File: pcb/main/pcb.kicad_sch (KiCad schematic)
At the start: 45 parts, among them J1 Conn_01x04, J2 USB_B_Micro, J6 Barrel_Jack_MountingPin, Q1 Q_NMOS_GDS, Q3 Q_NMOS_GDS, U2 ESP32-C3-WROOM-02, U5 IX4427N, U6 LMR54406DBVR

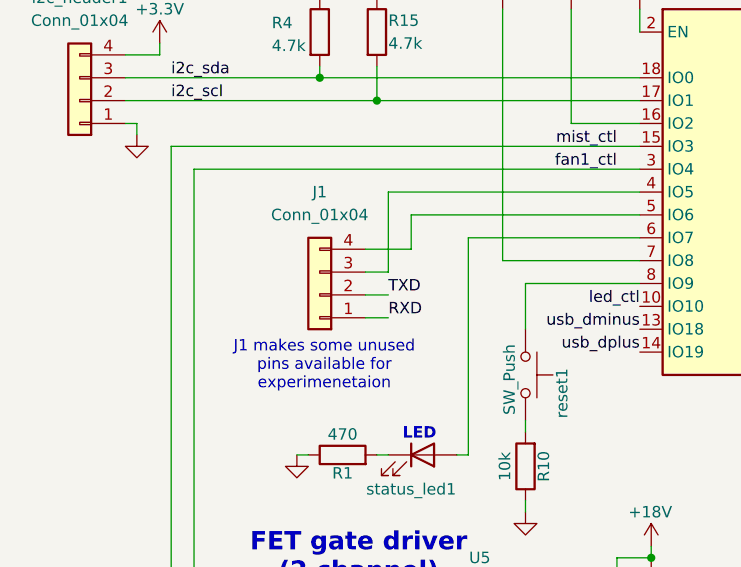
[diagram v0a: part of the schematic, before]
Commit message: pcb: mark debug header as "do not place" and add a part number for i2c header
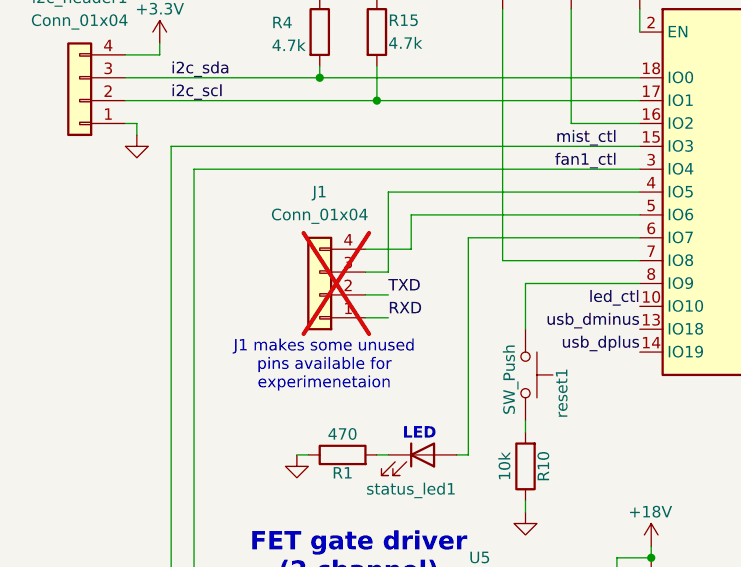
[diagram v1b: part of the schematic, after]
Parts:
- J1: now not fitted; now left out of the parts list
- i2c_header1: LCSC Part # (none) -> C124378
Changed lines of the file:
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@@
+			)
+		)
+		(property "LCSC Part #" "C124378"
+			(at 27.94 83.82 0)
+			(effects
+				(font
+					(size 1.27 1.27)
+				)
+				(hide yes)
 			)
 		)
@@
 		(unit 1)
 		(exclude_from_sim no)
-		(in_bom yes)
-		(on_board yes)
-		(dnp no)
+		(in_bom no)
+		(on_board yes)
+		(dnp yes)
 		(fields_autoplaced yes)
 		(property "Reference" "J1"

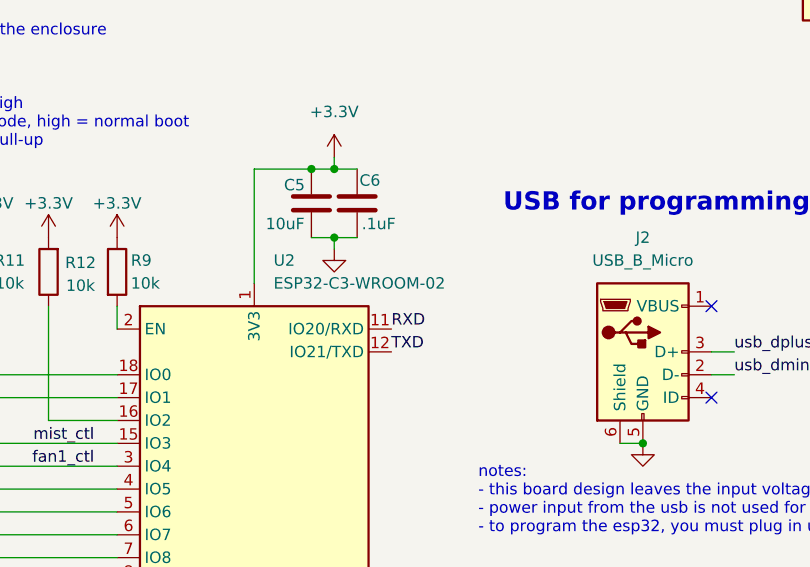
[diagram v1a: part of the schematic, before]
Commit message: pcb: update part # for esp32
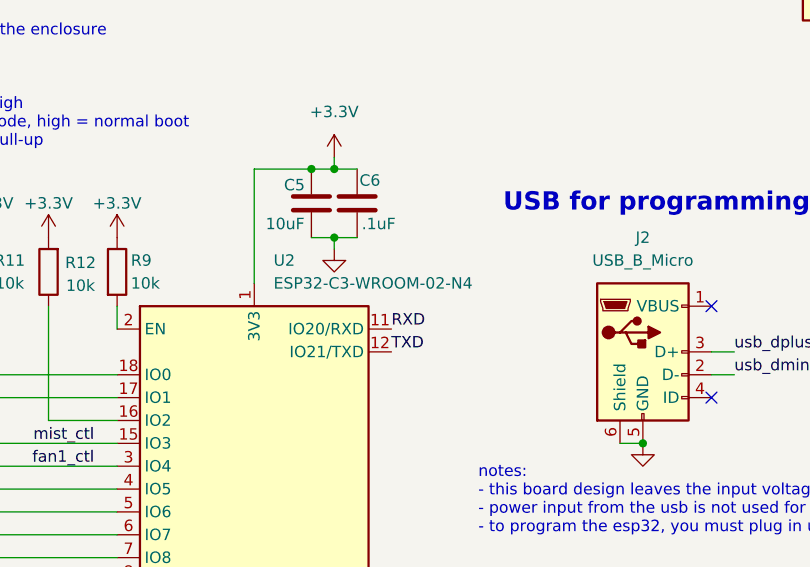
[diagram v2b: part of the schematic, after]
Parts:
- U2: value ESP32-C3-WROOM-02 -> ESP32-C3-WROOM-02-N4; LCSC Part # (none) -> C2934560
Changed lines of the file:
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@@
 			)
 		)
-		(property "Value" "ESP32-C3-WROOM-02"
+		(property "Value" "ESP32-C3-WROOM-02-N4"
 			(at 107.5533 71.12 0)
 			(effects
@@
 			)
 		)
+		(property "LCSC Part #" "C2934560"
+			(at 105.41 93.98 0)
+			(effects
+				(font
+					(size 1.27 1.27)
+				)
+				(hide yes)
+			)
+		)
